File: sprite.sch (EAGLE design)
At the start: 40 parts

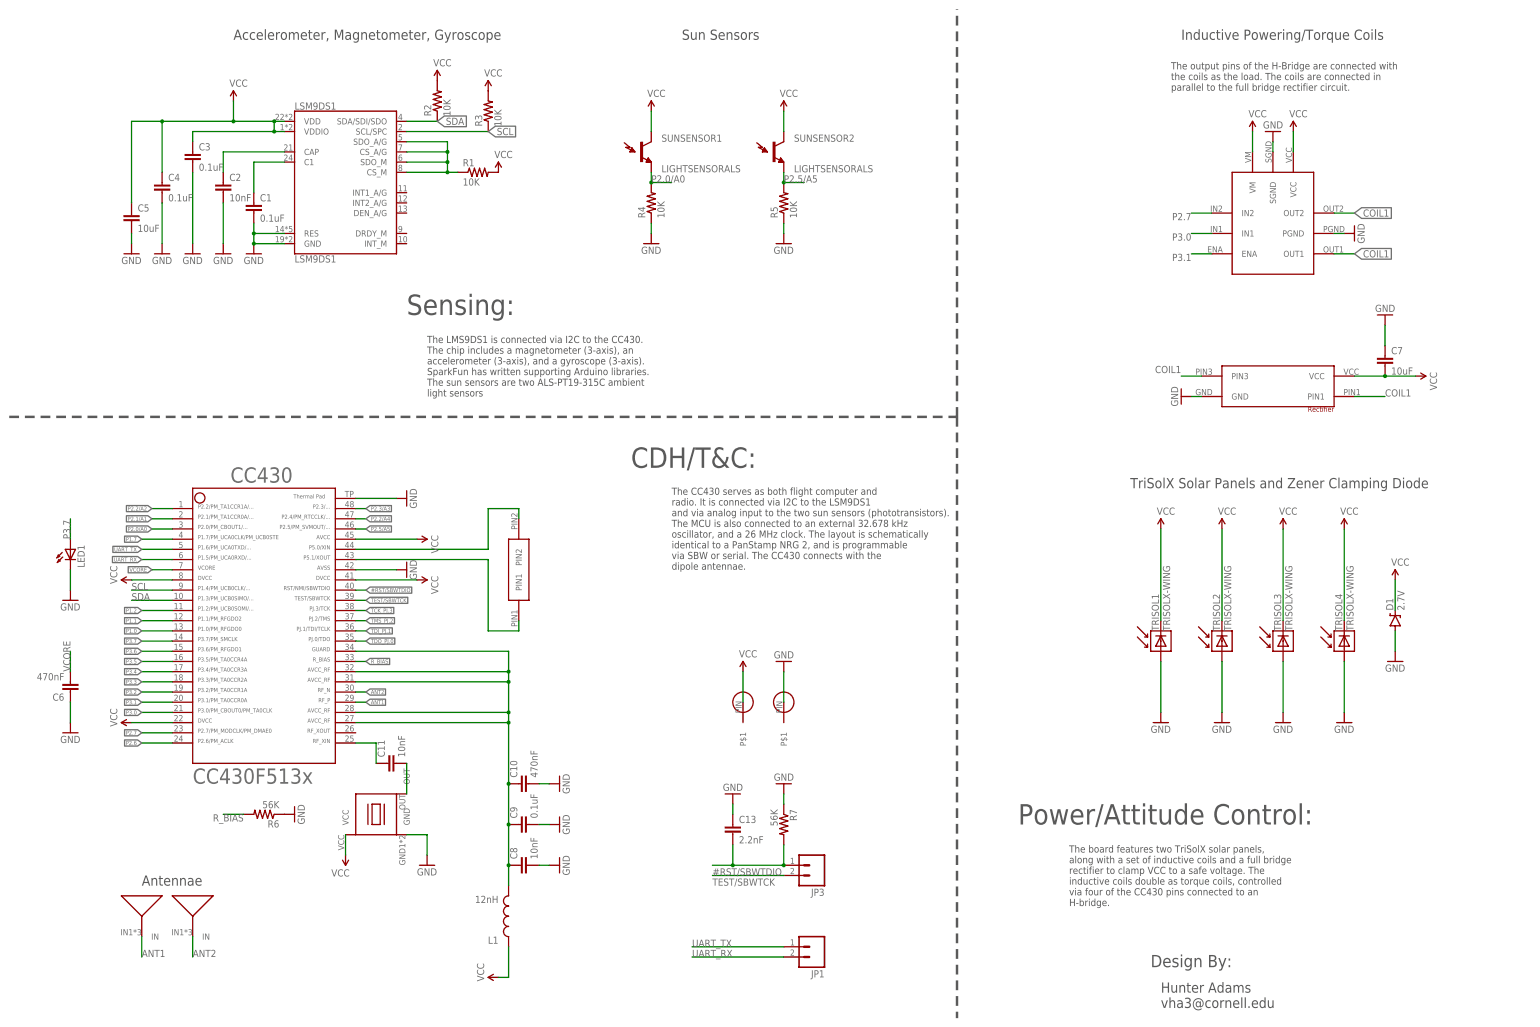
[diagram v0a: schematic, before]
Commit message: fixed reset line, added current-limiting resistor and bypass cap
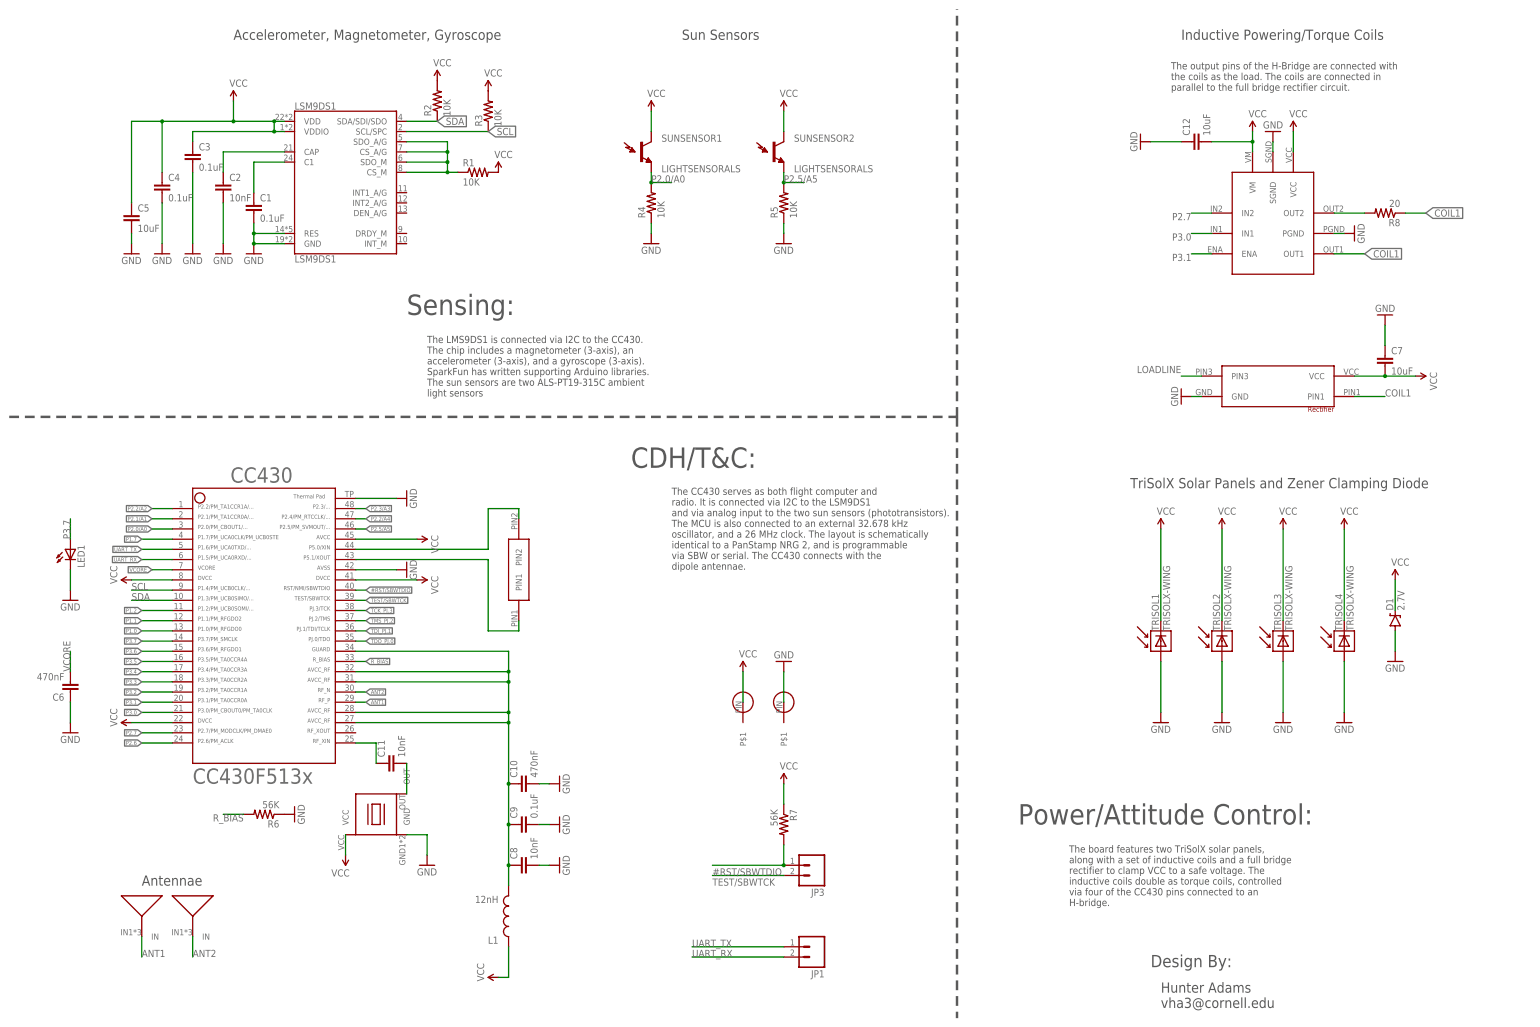
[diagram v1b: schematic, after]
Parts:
- removed C13: 2.2nF, SparkFun:CAP0805
- added C12: 10uF, SparkFun:CAP0805
- added R8: 20, SparkFun:RESISTOR0805-RES
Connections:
- new net LOADLINE: H-BRIDGE.OUT2, R8.2, RECTIFIER.PIN3
- net #RST/SBWTDIO: no longer C13.2
- net COIL1: now also R8.1; no longer H-BRIDGE.OUT2, RECTIFIER.PIN3
- net GND: now also C12.1; no longer C13.1, R7.1
- net VCC: now also C12.2, R7.1
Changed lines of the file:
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@@
 <part name="P+17" library="SparkFun" deviceset="VCC" device=""/>
 <part name="JP3" library="SparkFun" deviceset="M02" device="PTH"/>
-<part name="C13" library="SparkFun" deviceset="CAP" device="0805" value="2.2nF"/>
 <part name="R7" library="SparkFun" deviceset="RESISTOR" device="0805-RES" value="56K"/>
-<part name="GND27" library="SparkFun" deviceset="GND" device=""/>
-<part name="GND28" library="SparkFun" deviceset="GND" device=""/>
 <part name="JP1" library="SparkFun" deviceset="M02" device="PTH"/>
 <part name="TRISOL2" library="TriSolX_QzQube" deviceset="TRISOLX-WING" device=""/>
@@
 <part name="GND19" library="SparkFun" deviceset="GND" device=""/>
 <part name="P+16" library="SparkFun" deviceset="VCC" device=""/>
+<part name="P+22" library="SparkFun" deviceset="VCC" device=""/>
+<part name="R8" library="SparkFun" deviceset="RESISTOR" device="0805-RES" value="20"/>
+<part name="C12" library="SparkFun" deviceset="CAP" device="0805" value="10uF"/>
+<part name="GND20" library="SparkFun" deviceset="GND" device=""/>
 </parts>
 <sheets>
@@
 <instance part="P+17" gate="1" x="187.96" y="91.44"/>
 <instance part="JP3" gate="G$1" x="205.74" y="43.18" rot="R180"/>
-<instance part="C13" gate="G$1" x="185.42" y="50.8"/>
 <instance part="R7" gate="G$1" x="198.12" y="53.34" rot="R270"/>
-<instance part="GND27" gate="1" x="185.42" y="60.96" rot="R180"/>
-<instance part="GND28" gate="1" x="198.12" y="63.5" rot="R180"/>
 <instance part="JP1" gate="G$1" x="205.74" y="22.86" rot="R180"/>
 <instance part="TRISOL2" gate="G$1" x="307.34" y="99.06" rot="R90"/>
@@
 <instance part="GND19" gate="1" x="109.22" y="43.18"/>
 <instance part="P+16" gate="1" x="88.9" y="45.72" rot="R180"/>
+<instance part="P+22" gate="1" x="198.12" y="63.5"/>
+<instance part="R8" gate="G$1" x="347.98" y="205.74" rot="R180"/>
+<instance part="C12" gate="G$1" x="302.26" y="223.52" rot="R90"/>
+<instance part="GND20" gate="1" x="287.02" y="223.52" rot="R270"/>
 </instances>
 <busses>
@@
 </segment>
 <segment>
-<pinref part="GND27" gate="1" pin="GND"/>
-<pinref part="C13" gate="G$1" pin="1"/>
-<wire x1="185.42" y1="58.42" x2="185.42" y2="55.88" width="0.1524" layer="91"/>
-</segment>
-<segment>
-<pinref part="GND28" gate="1" pin="GND"/>
-<pinref part="R7" gate="G$1" pin="1"/>
-<wire x1="198.12" y1="60.96" x2="198.12" y2="58.42" width="0.1524" layer="91"/>
-</segment>
-<segment>
 <pinref part="TRISOL2" gate="G$1" pin="A"/>
 <pinref part="GND29" gate="1" pin="GND"/>
@@
 <wire x1="104.14" y1="50.8" x2="109.22" y2="50.8" width="0.1524" layer="91"/>
 <wire x1="109.22" y1="50.8" x2="109.22" y2="45.72" width="0.1524" layer="91"/>
+</segment>
+<segment>
+<pinref part="GND20" gate="1" pin="GND"/>
+<pinref part="C12" gate="G$1" pin="1"/>
+<wire x1="289.56" y1="223.52" x2="297.18" y2="223.52" width="0.1524" layer="91"/>
 </segment>
 </net>
@@
 <pinref part="P+14" gate="1" pin="VCC"/>
 <pinref part="H-BRIDGE" gate="G$1" pin="VM"/>
-<wire x1="314.96" y1="226.06" x2="314.96" y2="220.98" width="0.1524" layer="91"/>
+<wire x1="314.96" y1="226.06" x2="314.96" y2="223.52" width="0.1524" layer="91"/>
+<pinref part="C12" gate="G$1" pin="2"/>
+<wire x1="314.96" y1="223.52" x2="314.96" y2="220.98" width="0.1524" layer="91"/>
+<wire x1="304.8" y1="223.52" x2="314.96" y2="223.52" width="0.1524" layer="91"/>
+<junction x="314.96" y="223.52"/>
 </segment>
 <segment>
@@
 <pinref part="P+16" gate="1" pin="VCC"/>
 <wire x1="88.9" y1="50.8" x2="88.9" y2="45.72" width="0.1524" layer="91"/>
+</segment>
+<segment>
+<pinref part="R7" gate="G$1" pin="1"/>
+<pinref part="P+22" gate="1" pin="VCC"/>
+<wire x1="198.12" y1="63.5" x2="198.12" y2="58.42" width="0.1524" layer="91"/>
 </segment>
 </net>
@@
 <segment>
 <pinref part="JP3" gate="G$1" pin="1"/>
-<wire x1="198.12" y1="43.18" x2="185.42" y2="43.18" width="0.1524" layer="91"/>
+<wire x1="198.12" y1="43.18" x2="180.34" y2="43.18" width="0.1524" layer="91"/>
 <label x="180.34" y="40.64" size="1.778" layer="95"/>
-<pinref part="C13" gate="G$1" pin="2"/>
-<wire x1="185.42" y1="43.18" x2="180.34" y2="43.18" width="0.1524" layer="91"/>
-<wire x1="185.42" y1="48.26" x2="185.42" y2="43.18" width="0.1524" layer="91"/>
-<junction x="185.42" y="43.18"/>
 <pinref part="R7" gate="G$1" pin="2"/>
 <wire x1="198.12" y1="48.26" x2="198.12" y2="43.18" width="0.1524" layer="91"/>
@@
 <segment>
 <pinref part="H-BRIDGE" gate="G$1" pin="OUT1"/>
-<wire x1="335.28" y1="195.58" x2="340.36" y2="195.58" width="0.1524" layer="91"/>
-<label x="340.36" y="195.58" size="1.778" layer="95" xref="yes"/>
+<wire x1="335.28" y1="195.58" x2="342.9" y2="195.58" width="0.1524" layer="91"/>
+<label x="342.9" y="195.58" size="1.778" layer="95" xref="yes"/>
 </segment>
 <segment>
@@
 </segment>
 <segment>
-<pinref part="RECTIFIER" gate="G$1" pin="PIN3"/>
-<wire x1="302.26" y1="165.1" x2="297.18" y2="165.1" width="0.1524" layer="91"/>
-<label x="297.18" y="167.64" size="1.778" layer="95" rot="R180"/>
-</segment>
-<segment>
-<pinref part="H-BRIDGE" gate="G$1" pin="OUT2"/>
-<wire x1="335.28" y1="205.74" x2="340.36" y2="205.74" width="0.1524" layer="91"/>
-<label x="340.36" y="205.74" size="1.778" layer="95" xref="yes"/>
+<pinref part="R8" gate="G$1" pin="1"/>
+<wire x1="353.06" y1="205.74" x2="358.14" y2="205.74" width="0.1524" layer="91"/>
+<label x="358.14" y="205.74" size="1.778" layer="95" xref="yes"/>
 </segment>
 </net>
@@
 </segment>
 </net>
+<net name="LOADLINE" class="0">
+<segment>
+<pinref part="RECTIFIER" gate="G$1" pin="PIN3"/>
+<wire x1="302.26" y1="165.1" x2="297.18" y2="165.1" width="0.1524" layer="91"/>
+<label x="297.18" y="167.64" size="1.778" layer="95" rot="R180"/>
+</segment>
+<segment>
+<pinref part="H-BRIDGE" gate="G$1" pin="OUT2"/>
+<pinref part="R8" gate="G$1" pin="2"/>
+<wire x1="335.28" y1="205.74" x2="342.9" y2="205.74" width="0.1524" layer="91"/>
+</segment>
+</net>

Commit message: updated gerbers
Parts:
- added R9: 5.6K, SparkFun:RESISTOR0805-RES
- D1: value 2.7V -> 2.2V
- R8: value 20 -> 1K
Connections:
- new net N$6: R9.1, VCCPIN.P$1
- net VCC: now also R9.2; no longer VCCPIN.P$1
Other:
- note added: "The board features four TriSolX solar panels, along with a set of inductive coils and a full bridge rectifier to clamp VCC to a safe voltage. The inductive coils double as torque coils, controlled via four of the CC430 pins connected to an H-bridge."
- note removed: "The board features two TriSolX solar panels, along with a set of inductive coils and a full bridge rectifier to clamp VCC to a safe voltage. The inductive coils double as torque coils, controlled via four of the CC430 pins connected to an H-bridge."
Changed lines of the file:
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@@
 <part name="C10" library="SparkFun" deviceset="CAP" device="0805" value="470nF"/>
 <part name="GND16" library="SparkFun" deviceset="GND" device=""/>
-<part name="D1" library="SparkFun-DiscreteSemi" deviceset="DIODE-ZENER" device="3.3V" value="2.7V"/>
+<part name="D1" library="SparkFun-DiscreteSemi" deviceset="DIODE-ZENER" device="3.3V" value="2.2V"/>
 <part name="P+11" library="SparkFun" deviceset="VCC" device=""/>
 <part name="GND13" library="SparkFun" deviceset="GND" device=""/>
@@
 <part name="P+16" library="SparkFun" deviceset="VCC" device=""/>
 <part name="P+22" library="SparkFun" deviceset="VCC" device=""/>
-<part name="R8" library="SparkFun" deviceset="RESISTOR" device="0805-RES" value="20"/>
+<part name="R8" library="SparkFun" deviceset="RESISTOR" device="0805-RES" value="1K"/>
 <part name="C12" library="SparkFun" deviceset="CAP" device="0805" value="10uF"/>
 <part name="GND20" library="SparkFun" deviceset="GND" device=""/>
+<part name="R9" library="SparkFun" deviceset="RESISTOR" device="0805-RES" value="5.6K"/>
 </parts>
 <sheets>
@@
 dipole antennae.</text>
 <text x="256.54" y="53.34" size="5.08" layer="97">Power/Attitude Control:</text>
-<text x="269.24" y="33.02" size="1.778" layer="97">The board features two TriSolX solar panels,
+<text x="269.24" y="33.02" size="1.778" layer="97">The board features four TriSolX solar panels,
 along with a set of inductive coils and a full bridge
 rectifier to clamp VCC to a safe voltage. The
@@
 <instance part="VCCPIN" gate="G$1" x="187.96" y="83.82" rot="R270"/>
 <instance part="GNDPIN" gate="G$1" x="198.12" y="83.82" rot="R270"/>
-<instance part="GND26" gate="1" x="198.12" y="93.98" rot="R180"/>
-<instance part="P+17" gate="1" x="187.96" y="91.44"/>
+<instance part="GND26" gate="1" x="198.12" y="106.68" rot="R180"/>
+<instance part="P+17" gate="1" x="187.96" y="104.14"/>
 <instance part="JP3" gate="G$1" x="205.74" y="43.18" rot="R180"/>
 <instance part="R7" gate="G$1" x="198.12" y="53.34" rot="R270"/>
@@
 <instance part="C12" gate="G$1" x="302.26" y="223.52" rot="R90"/>
 <instance part="GND20" gate="1" x="287.02" y="223.52" rot="R270"/>
+<instance part="R9" gate="G$1" x="187.96" y="93.98" rot="R90"/>
 </instances>
 <busses>
@@
 <pinref part="GND26" gate="1" pin="GND"/>
 <pinref part="GNDPIN" gate="G$1" pin="P$1"/>
-<wire x1="198.12" y1="91.44" x2="198.12" y2="83.82" width="0.1524" layer="91"/>
+<wire x1="198.12" y1="104.14" x2="198.12" y2="83.82" width="0.1524" layer="91"/>
 </segment>
 <segment>
@@
 </segment>
 <segment>
-<pinref part="P+17" gate="1" pin="VCC"/>
-<pinref part="VCCPIN" gate="G$1" pin="P$1"/>
-<wire x1="187.96" y1="91.44" x2="187.96" y2="83.82" width="0.1524" layer="91"/>
-</segment>
-<segment>
 <pinref part="P+18" gate="1" pin="VCC"/>
 <pinref part="TRISOL2" gate="G$1" pin="C"/>
@@
 <pinref part="P+22" gate="1" pin="VCC"/>
 <wire x1="198.12" y1="63.5" x2="198.12" y2="58.42" width="0.1524" layer="91"/>
+</segment>
+<segment>
+<pinref part="P+17" gate="1" pin="VCC"/>
+<pinref part="R9" gate="G$1" pin="2"/>
+<wire x1="187.96" y1="104.14" x2="187.96" y2="99.06" width="0.1524" layer="91"/>
 </segment>
 </net>
@@
 </segment>
 </net>
+<net name="N$6" class="0">
+<segment>
+<pinref part="VCCPIN" gate="G$1" pin="P$1"/>
+<pinref part="R9" gate="G$1" pin="1"/>
+<wire x1="187.96" y1="83.82" x2="187.96" y2="88.9" width="0.1524" layer="91"/>
+</segment>
+</net>
